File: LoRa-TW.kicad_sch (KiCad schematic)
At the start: 4 parts, among them U1 SX1262IMLTRT

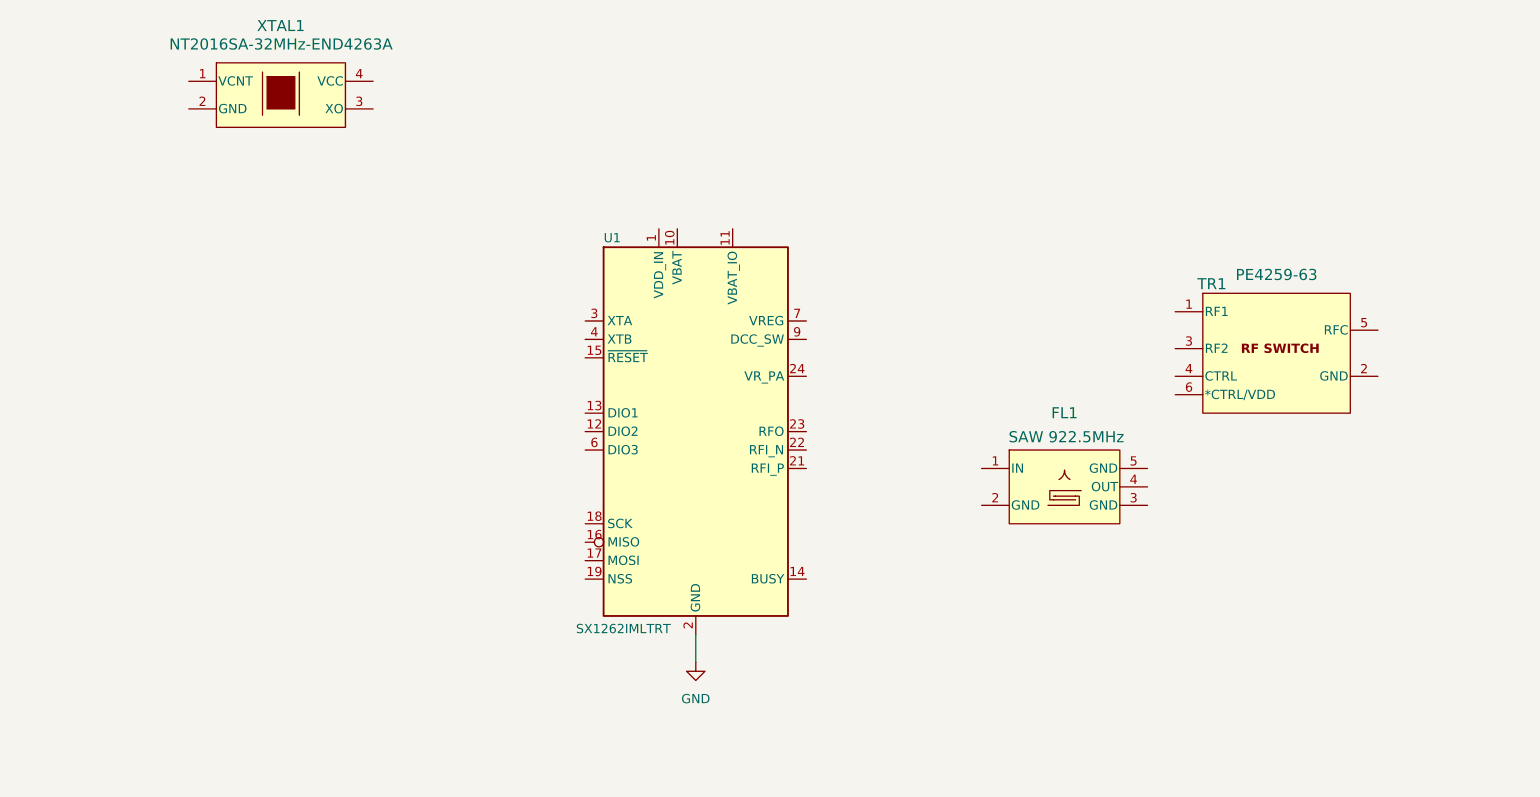
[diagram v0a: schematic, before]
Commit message: update receive of schematic
- update symbol
- place rx path components
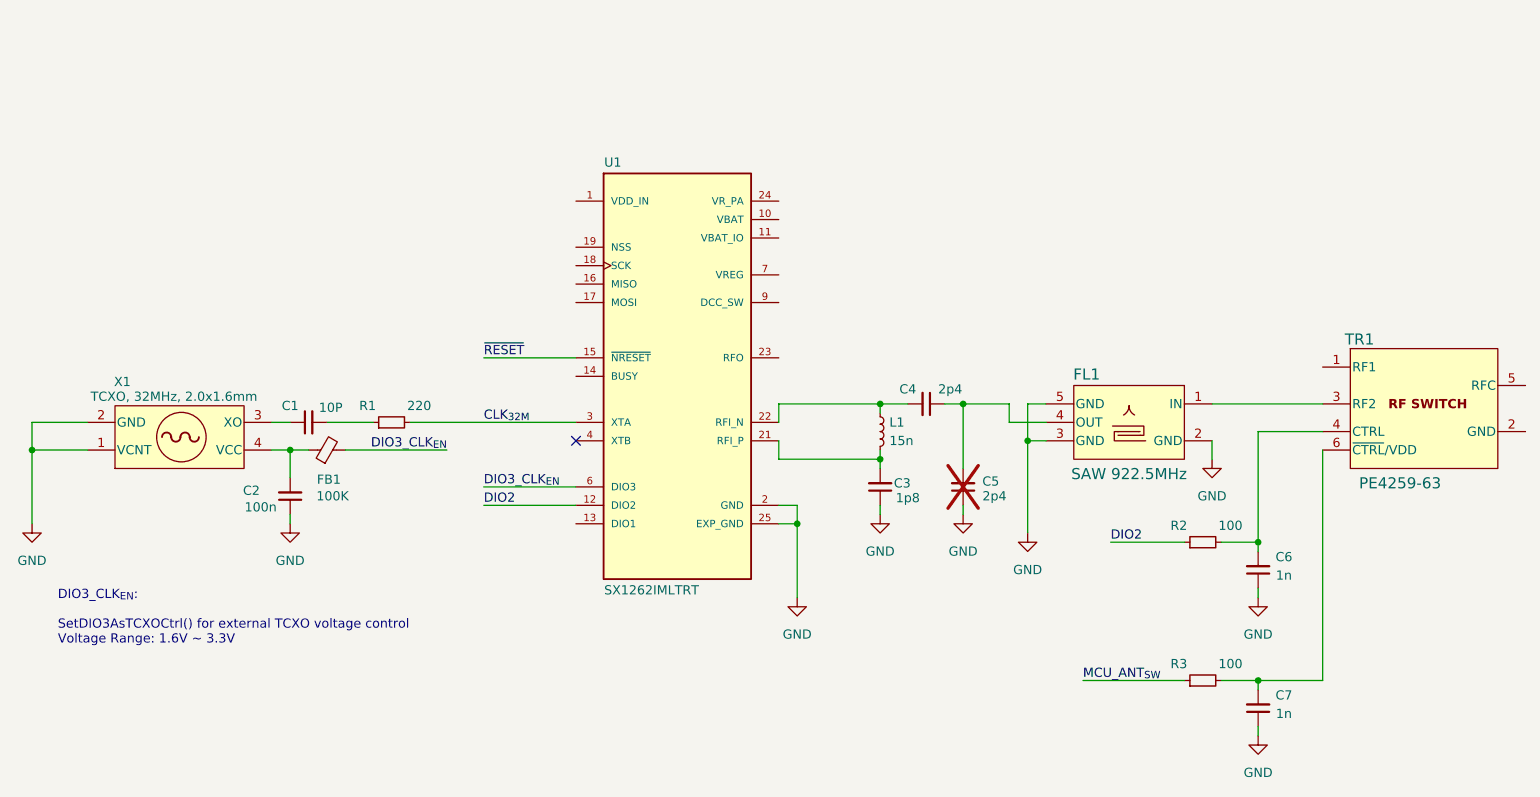
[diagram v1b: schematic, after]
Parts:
- removed U1: SX1262IMLTRT, Package_DFN_QFN:QFN-24-1EP_4x4mm_P0.5mm_EP2.6x2.6mm, symbol RF:SX1262IMLTRT
- added C1: 10P, Capacitor_SMD:C_0402_1005Metric, symbol Device:C_Small
- added C2: 100n, Capacitor_SMD:C_0402_1005Metric, symbol Device:C_Small
- added C3: 1p8, Capacitor_SMD:C_0402_1005Metric, symbol Device:C_Small
- added C4, C5: 2p4, Capacitor_SMD:C_0402_1005Metric, symbol Device:C_Small
- added C6, C7: 1n, Capacitor_SMD:C_0402_1005Metric, symbol Device:C_Small
- added FB1: 100K, Resistor_SMD:R_0402_1005Metric, symbol Device:FerriteBead_Small
- added L1: 15n, Inductor_SMD:L_0402_1005Metric, symbol Device:L_Small
- added R1: 220, Resistor_SMD:R_0402_1005Metric, symbol Device:R_Small
- added R2, R3: 100, Resistor_SMD:R_0402_1005Metric, symbol Device:R_Small
- added U1: SX1262IMLTRT, LoRa-TW:SX1262IMLTRT, symbol LoRa-TW:SX1262IMLTRT
- X1: renamed from XTAL1; value NT2016SA-32MHz-END4263A -> TCXO, 32MHz, 2.0x1.6mm
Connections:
- net GND: now also FL1.2 (GND), FL1.3 (GND), FL1.5 (GND), X1.1 (VCNT), X1.2 (GND), C2.1, C3.1, C5.1, C6.1, C7.1, U1.2 (GND), U1.20 (GND), U1.25 (EXP_GND), U1.5 (GND), U1.8 (GND)
- net at X1.3 (XO): now also C1.1
- net at X1.4 (VCC): now also C2.2, FB1.1
- net at TR1.3 (RF2): now also FL1.1 (IN)
- net at TR1.4 (CTRL): now also C6.2, R2.2
- net at TR1.6 (~{CTRL}/VDD): now also C7.2, R3.2
- net at FL1.4 (OUT): now also C4.1, C5.2
- new net: C4.2, L1.1, U1.22 (RFI_N)
- new net: C1.2, R1.1
- new net: C3.2, L1.2, U1.21 (RFI_P)
- new net CLK_{32M}: R1.2, U1.3 (XTA)
- new net DIO2: R2.1, U1.12 (DIO2)
- new net DIO3_CLK_{EN}: FB1.2, U1.6 (DIO3)
- new net MCU_ANT_{SW}: R3.1
- new net ~{RESET}: U1.15 (~{NRESET})
- no-connect marks 0 -> 1
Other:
- note added: "DIO3_CLK_{EN}: SetDIO3AsTCXOCtrl() for external TCXO voltage control Voltage Range: 1.6V ~ 3.3V"
- moved on the sheet: FL1, TR1
